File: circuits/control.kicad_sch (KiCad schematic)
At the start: 8 parts, among them Q1 Q_MMBT5551, Q2 Q_AO3400A, Q3 Q_MMBT5551, Q4 Q_AO3400A

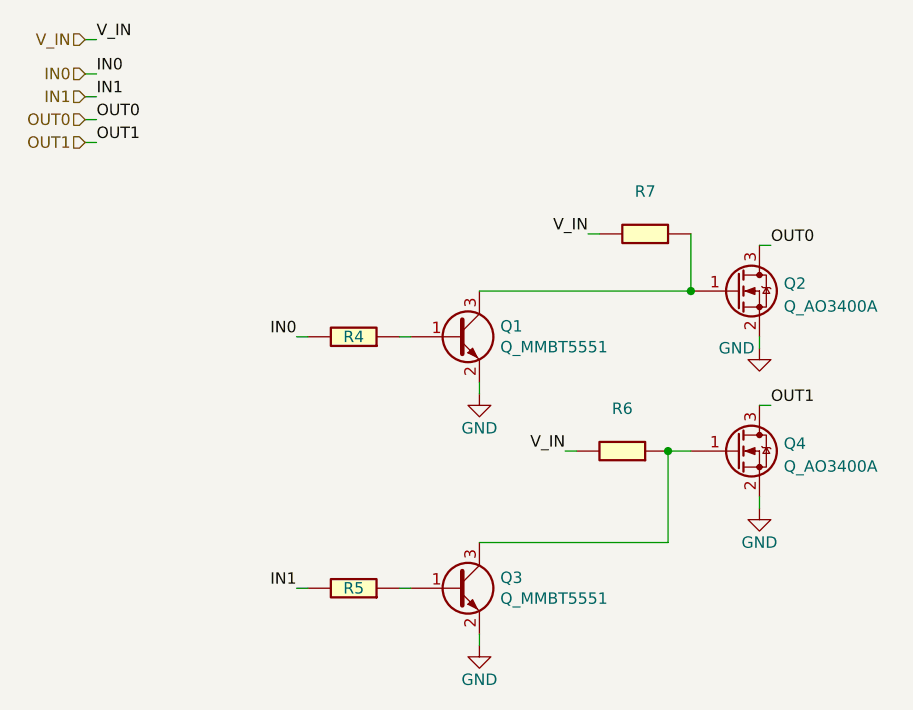
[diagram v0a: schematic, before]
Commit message: corrected footprints for manufacturer
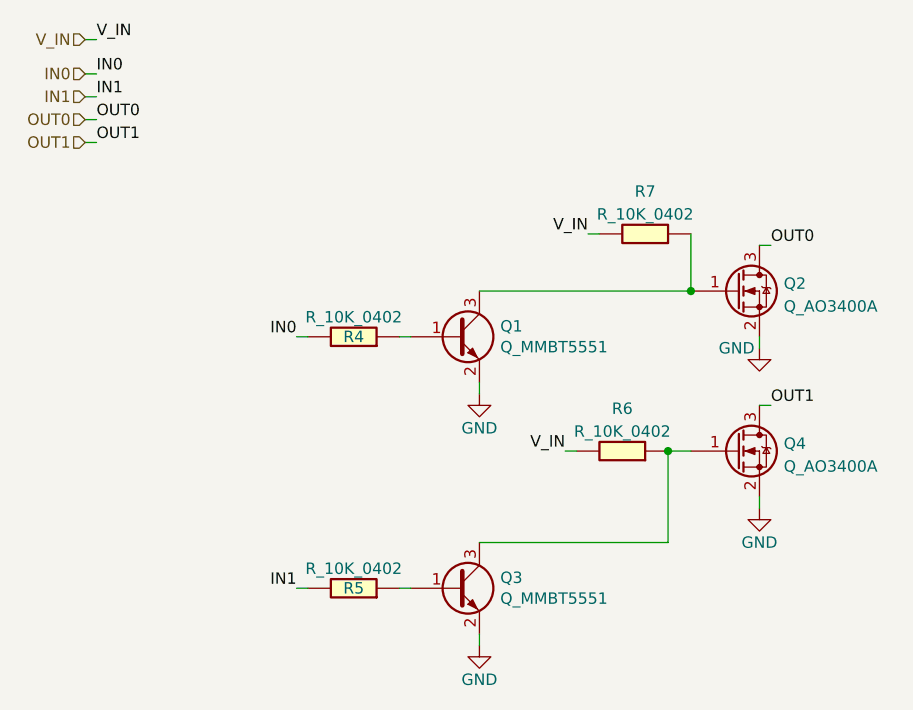
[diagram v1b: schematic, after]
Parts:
- R4, R5, R6, R7: value (none) -> R_10K_0402
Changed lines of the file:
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@@
     (in_bom yes) (on_board yes)
     (property "Reference" "R5" (id 0) (at 59.055 87.63 90))
-    (property "Value" "" (id 1) (at 59.055 85.4511 90))
+    (property "Value" "R_10K_0402" (id 1) (at 59.055 85.4511 90))
     (property "Footprint" "Resistor_SMD:R_0402_1005Metric_Pad0.72x0.64mm_HandSolder" (id 2) (at 59.055 89.408 90)
       (effects (font (size 1.27 1.27)) hide)
@@
     (in_bom yes) (on_board yes)
     (property "Reference" "R7" (id 0) (at 91.44 43.5442 90))
-    (property "Value" "" (id 1) (at 91.44 46.0811 90))
+    (property "Value" "R_10K_0402" (id 1) (at 91.44 46.0811 90))
     (property "Footprint" "Resistor_SMD:R_0402_1005Metric_Pad0.72x0.64mm_HandSolder" (id 2) (at 91.44 50.038 90)
       (effects (font (size 1.27 1.27)) hide)
@@
     (in_bom yes) (on_board yes)
     (property "Reference" "R4" (id 0) (at 59.055 59.69 90))
-    (property "Value" "" (id 1) (at 59.055 57.5111 90))
+    (property "Value" "R_10K_0402" (id 1) (at 59.055 57.5111 90))
     (property "Footprint" "Resistor_SMD:R_0402_1005Metric_Pad0.72x0.64mm_HandSolder" (id 2) (at 59.055 61.468 90)
       (effects (font (size 1.27 1.27)) hide)
@@
     (in_bom yes) (on_board yes)
     (property "Reference" "R6" (id 0) (at 88.9 67.6742 90))
-    (property "Value" "" (id 1) (at 88.9 70.2111 90))
+    (property "Value" "R_10K_0402" (id 1) (at 88.9 70.2111 90))
     (property "Footprint" "Resistor_SMD:R_0402_1005Metric_Pad0.72x0.64mm_HandSolder" (id 2) (at 88.9 74.168 90)
       (effects (font (size 1.27 1.27)) hide)
